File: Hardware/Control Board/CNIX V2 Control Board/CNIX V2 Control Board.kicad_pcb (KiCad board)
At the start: 2 copper layers, 165 x 51 mm, 108 parts, among them J1 EXT, J10 LED, J11 USB_C_Receptacle, J3 Tube Out, J4 EXT, J5 I2C_ext, J6 Prog, J7 HT, J8 GND, J9 GND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

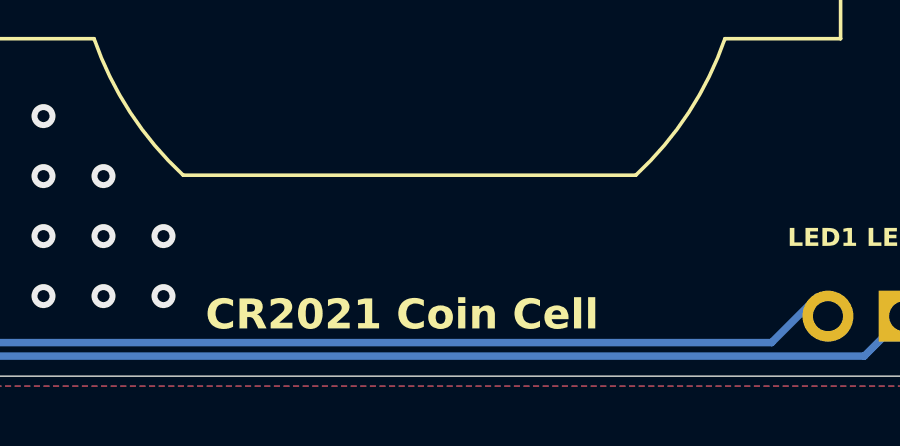
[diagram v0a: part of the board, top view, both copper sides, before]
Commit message: control board version 2.1.1 bump and added changelog
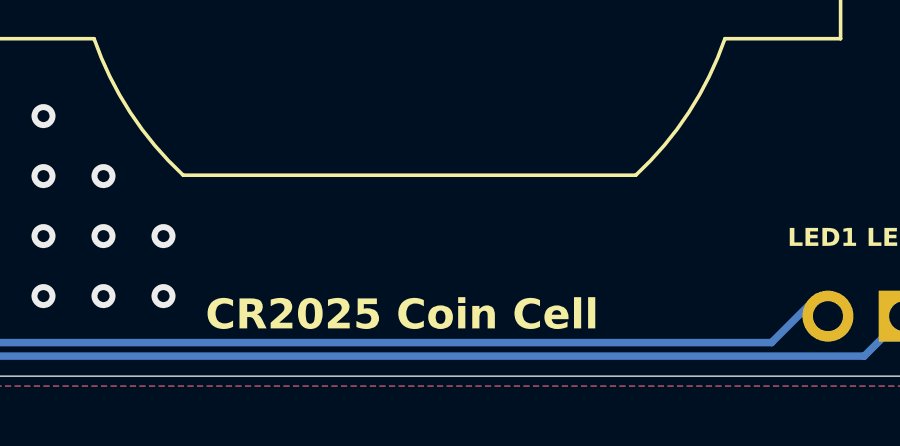
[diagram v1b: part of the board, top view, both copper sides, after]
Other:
- board text added: "CR2025 Coin Cell"
- board text removed: "CR2021 Coin Cell"
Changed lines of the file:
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@@
 	)
 	(paper "A4")
+	(title_block
+		(title "Nixie Tube Control Board")
+		(date "2026-01-13")
+		(rev "V2.1.1")
+		(company "C-Audio")
+	)
 	(layers
 		(0 "F.Cu" signal)
@@
 		)
 	)
-	(gr_text "CR2021 Coin Cell"
+	(gr_text "CR2025 Coin Cell"
 		(at 204.711051 129.531051 0)
 		(layer "F.SilkS" knockout)

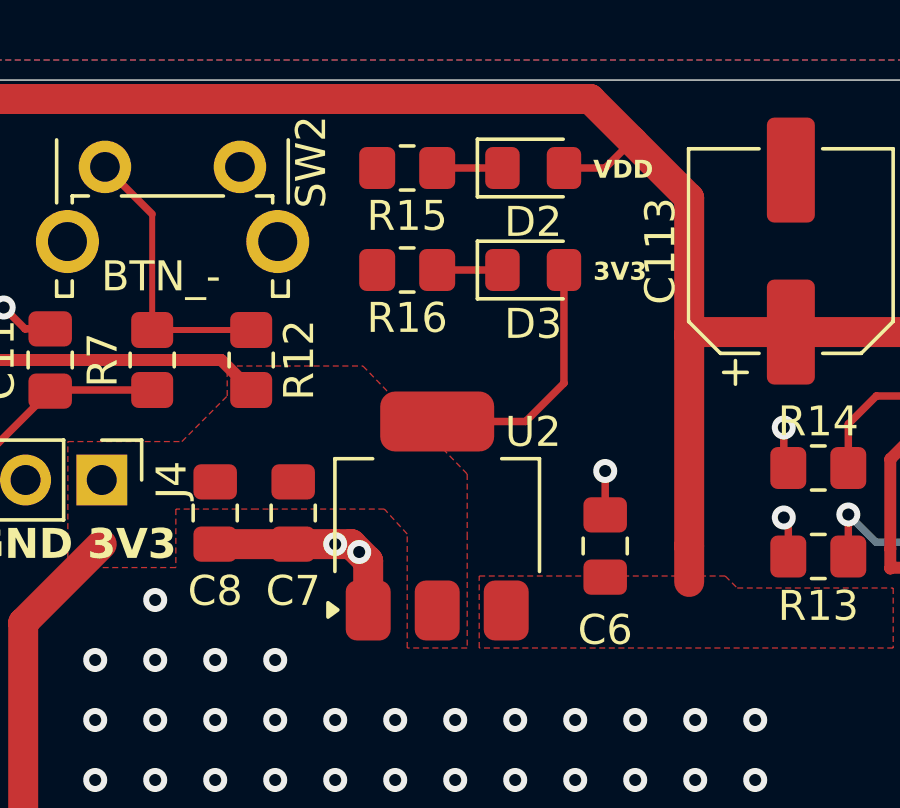
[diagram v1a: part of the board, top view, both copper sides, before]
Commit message: Version bump 2.2.0 -> new regulator and id system
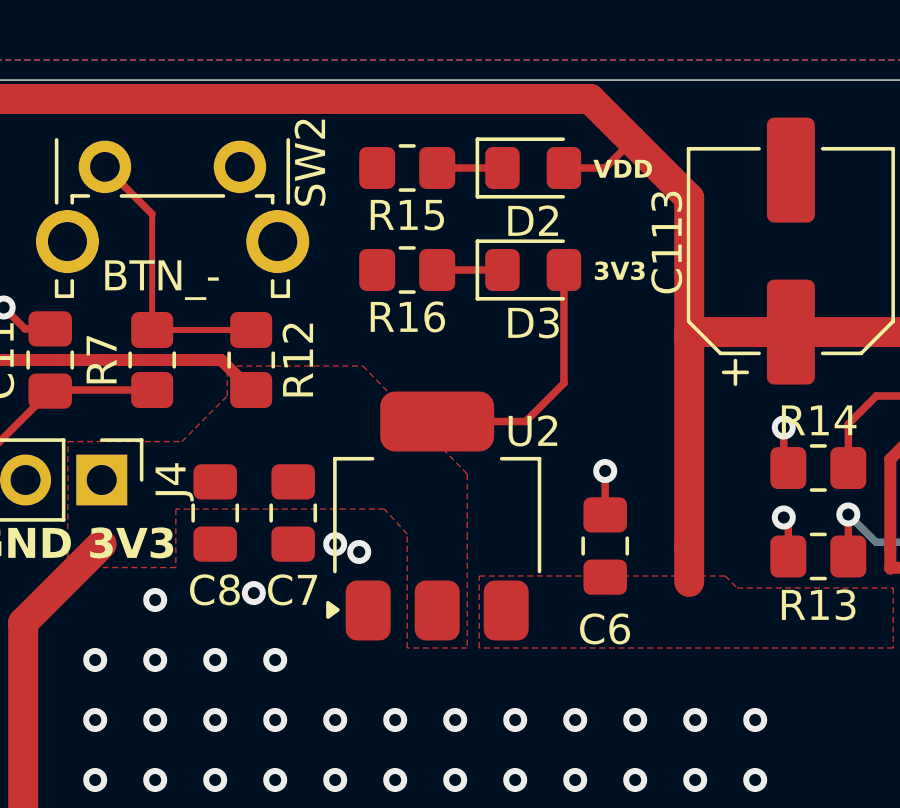
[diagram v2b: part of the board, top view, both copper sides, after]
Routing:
- net GND: track 63.8 -> 56.8 mm, vias 276 -> 277

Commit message: updated firmware: implemented DHT22 sensor, addon board id check, menu structure, led blink display
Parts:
- SW2: value SW_Plus -> SW_Minus
- SW4: value SW_Minus -> SW_Plus
- U2: value AMS1117-3.3 -> AP7361C-33ER-13
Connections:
- net /PD2 renamed /id_bit0
- net /PD3 renamed /id_bit1
- C11 pad 1: /btn_plus -> /btn_minus
- C9 pad 1: /btn_minus -> /btn_plus
- R7 pad 1: /btn_plus -> /btn_minus
- R9 pad 1: /btn_minus -> /btn_plus
- U1 pad 16: /btn_plus -> /btn_minus
- U1 pad 18: /btn_minus -> /btn_plus
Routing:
- net /btn_plus: track 36.9 -> 19.1 mm
- net /btn_minus: track 19.1 -> 36.9 mm
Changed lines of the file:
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@@
 	(net 79 "Net-(D102-A)")
 	(net 80 "Net-(D103-K)")
-	(net 81 "/PD2")
-	(net 82 "/PD3")
+	(net 81 "/id_bit0")
+	(net 82 "/id_bit1")
 	(footprint "TestPoint:TestPoint_Pad_D1.5mm"
 		(layer "F.Cu")
@@
 			(layers "F.Cu" "F.Mask" "F.Paste")
 			(roundrect_rratio 0.208333)
-			(net 13 "/btn_plus")
+			(net 15 "/btn_minus")
 			(pintype "passive")
 		)
@@
 			(layers "F.Cu" "F.Mask" "F.Paste")
 			(roundrect_rratio 0.212766)
-			(net 13 "/btn_plus")
+			(net 15 "/btn_minus")
 			(pintype "passive")
 		)
@@
 			)
 		)
-		(property "Value" "SW_Plus"
+		(property "Value" "SW_Minus"
 			(at 2.25 5.38988 0)
 			(layer "F.Fab")
@@
 			(layers "F.Cu" "F.Mask" "F.Paste")
 			(roundrect_rratio 0.212766)
-			(net 15 "/btn_minus")
+			(net 13 "/btn_plus")
 			(pintype "passive")
 		)
@@
 			(layers "F.Cu" "F.Mask" "F.Paste")
 			(roundrect_rratio 0.208333)
-			(net 15 "/btn_minus")
+			(net 13 "/btn_plus")
 			(pintype "passive")
 		)
@@
 			(layers "F.Cu" "F.Mask" "F.Paste")
 			(roundrect_rratio 0.25)
-			(net 13 "/btn_plus")
+			(net 15 "/btn_minus")
 			(pinfunction "PA5")
 			(pintype "bidirectional")
@@
 			(layers "F.Cu" "F.Mask" "F.Paste")
 			(roundrect_rratio 0.25)
-			(net 15 "/btn_minus")
+			(net 13 "/btn_plus")
 			(pinfunction "PA7")
 			(pintype "bidirectional")
@@
 			(layers "F.Cu" "F.Mask" "F.Paste")
 			(roundrect_rratio 0.25)
-			(net 81 "/PD2")
+			(net 81 "/id_bit0")
 			(pinfunction "PD2")
 			(pintype "bidirectional")
@@
 			(layers "F.Cu" "F.Mask" "F.Paste")
 			(roundrect_rratio 0.25)
-			(net 82 "/PD3")
+			(net 82 "/id_bit1")
 			(pinfunction "PD3")
 			(pintype "bidirectional")
@@
 			)
 		)
-		(property "Value" "SW_Minus"
+		(property "Value" "SW_Plus"
 			(at 2.25 5.38988 0)
 			(layer "F.Fab")
@@
 			)
 		)
-		(property "Value" "AMS1117-3.3"
+		(property "Value" "AP7361C-33ER-13"
 			(at 0 4.500001 90)
 			(layer "F.Fab")
@@
 			)
 		)
-		(property "Datasheet" "http://www.advanced-monolithic.com/pdf/ds1117.pdf"
+		(property "Datasheet" "https://www.mouser.de/datasheet/3/175/1/AP7361C.pdf"
 			(at 0 0 90)
 			(unlocked yes)
@@
 			)
 		)
-		(property "Description" "1A Low Dropout regulator, positive, 3.3V fixed output, SOT-223"
+		(property "Description" "The AP7361C is a 1A, adjustable and fixed output voltage, ultra-low dropout linear regulator with enable. The device includes pass element, error amplifier, band-gap reference, current limit and thermal shutdown circuitry. The device is turned on when EN pin is set to logic high level."
 			(at 0 0 90)
 			(unlocked yes)
@@
 			)
 		)
-		(property "Mouser-Nr." ""
+		(property "Mouser-Nr." "621-AP7361C-33ER-13 "
 			(at 0 0 90)
 			(unlocked yes)
@@
 			(layers "*.Cu" "*.Mask")
 			(remove_unused_layers no)
-			(net 81 "/PD2")
+			(net 81 "/id_bit0")
 			(pinfunction "Pin_3")
 			(pintype "passive")
@@
 			(layers "*.Cu" "*.Mask")
 			(remove_unused_layers no)
-			(net 82 "/PD3")
+			(net 82 "/id_bit1")
 			(pinfunction "Pin_4")
 			(pintype "passive")
@@
 	)
 	(segment
-		(start 176.622447 92.156051)
-		(end 176.311051 92.467447)
-		(width 0.25)
-		(layer "F.Cu")
-		(net 13)
-	)
-	(segment
-		(start 176.311051 103.498817)
-		(end 174.138266 105.671602)
+		(start 174.811051 91.831051)
+		(end 175.411051 92.431051)
 		(width 0.25)
 		(layer "F.Cu")
@@
 	)
 	(segment
-		(start 198.211051 90.331051)
-		(end 194.848551 90.331051)
+		(start 171.411051 90.368551)
+		(end 174.773551 90.368551)
 		(width 0.25)
 		(layer "F.Cu")
@@
 	)
 	(segment
-		(start 193.023551 92.156051)
-		(end 176.622447 92.156051)
+		(start 174.773551 90.368551)
+		(end 174.811051 90.331051)
 		(width 0.25)
 		(layer "F.Cu")
@@
 	)
 	(segment
-		(start 176.311051 92.467447)
-		(end 176.311051 103.498817)
+		(start 175.411051 102.984605)
+		(end 173.43116 104.964496)
 		(width 0.25)
 		(layer "F.Cu")
@@
 	)
 	(segment
-		(start 194.848551 90.331051)
-		(end 194.811051 90.368551)
+		(start 174.811051 90.331051)
+		(end 174.811051 91.831051)
 		(width 0.25)
 		(layer "F.Cu")
@@
 	)
 	(segment
-		(start 194.811051 90.368551)
-		(end 193.023551 92.156051)
+		(start 175.411051 92.431051)
+		(end 175.411051 102.984605)
 		(width 0.25)
 		(layer "F.Cu")
@@
 	)
 	(segment
-		(start 174.811051 91.831051)
-		(end 175.411051 92.431051)
+		(start 176.622447 92.156051)
+		(end 176.311051 92.467447)
 		(width 0.25)
 		(layer "F.Cu")
@@
 	)
 	(segment
-		(start 171.411051 90.368551)
-		(end 174.773551 90.368551)
+		(start 176.311051 103.498817)
+		(end 174.138266 105.671602)
 		(width 0.25)
 		(layer "F.Cu")
@@
 	)
 	(segment
-		(start 174.773551 90.368551)
-		(end 174.811051 90.331051)
+		(start 198.211051 90.331051)
+		(end 194.848551 90.331051)
 		(width 0.25)
 		(layer "F.Cu")
@@
 	)
 	(segment
-		(start 175.411051 102.984605)
-		(end 173.43116 104.964496)
+		(start 193.023551 92.156051)
+		(end 176.622447 92.156051)
 		(width 0.25)
 		(layer "F.Cu")
@@
 	)
 	(segment
-		(start 174.811051 90.331051)
-		(end 174.811051 91.831051)
+		(start 176.311051 92.467447)
+		(end 176.311051 103.498817)
 		(width 0.25)
 		(layer "F.Cu")
@@
 	)
 	(segment
-		(start 175.411051 92.431051)
-		(end 175.411051 102.984605)
+		(start 194.848551 90.331051)
+		(end 194.811051 90.368551)
+		(width 0.25)
+		(layer "F.Cu")
+		(net 15)
+	)
+	(segment
+		(start 194.811051 90.368551)
+		(end 193.023551 92.156051)
 		(width 0.25)
 		(layer "F.Cu")

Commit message: control board: added ht-psu enable jumper
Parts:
- added J100: HT_en, Connector_PinHeader_2.54mm:PinHeader_1x02_P2.54mm_Vertical, F.Cu at (101.5, 84.2)
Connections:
- D103 pad 2: /EN -> /~{EN}
- R100 pad 1: /EN -> Net-(J100-Pin_1)
- TP3 pad 1: /EN -> /~{EN}
- U1 pad 11: /EN -> /~{EN}
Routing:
- net /EN: track 108.1 -> 0.00 mm, vias 2 -> 0
- net /~{EN}: track 0.00 -> 107.3 mm, vias 0 -> 2
- net Net-(J100-Pin_1): track 0.00 -> 5.86 mm
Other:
- board text added: "EN_Enable"

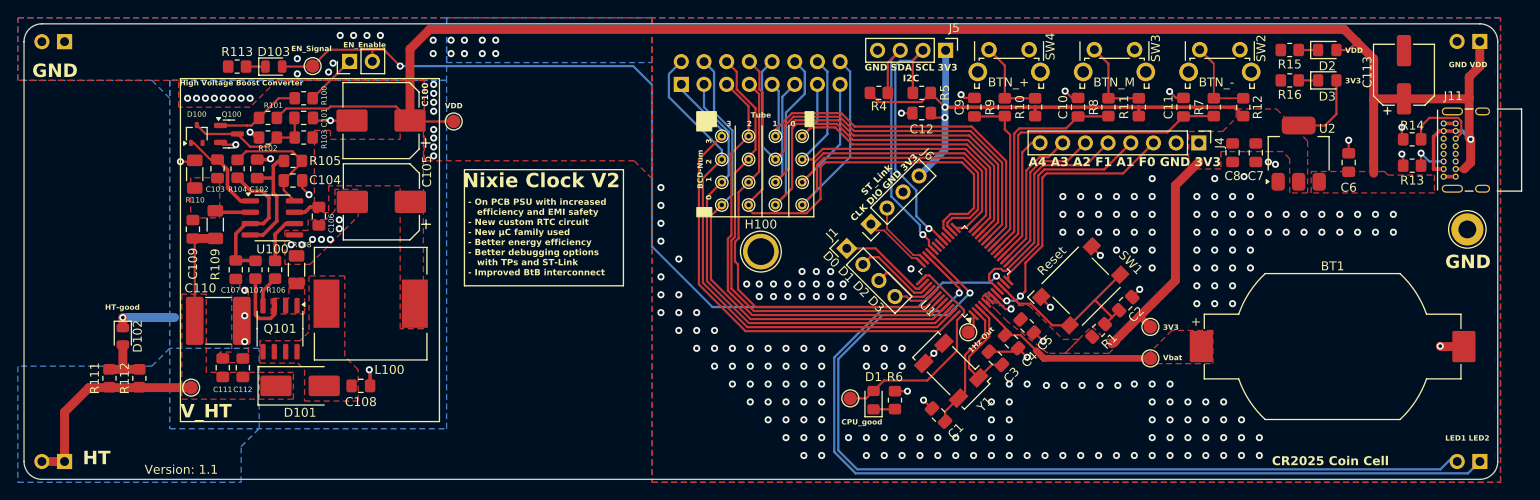
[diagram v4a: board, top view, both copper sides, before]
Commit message: finalized V2 and cleaned up Silkscreen
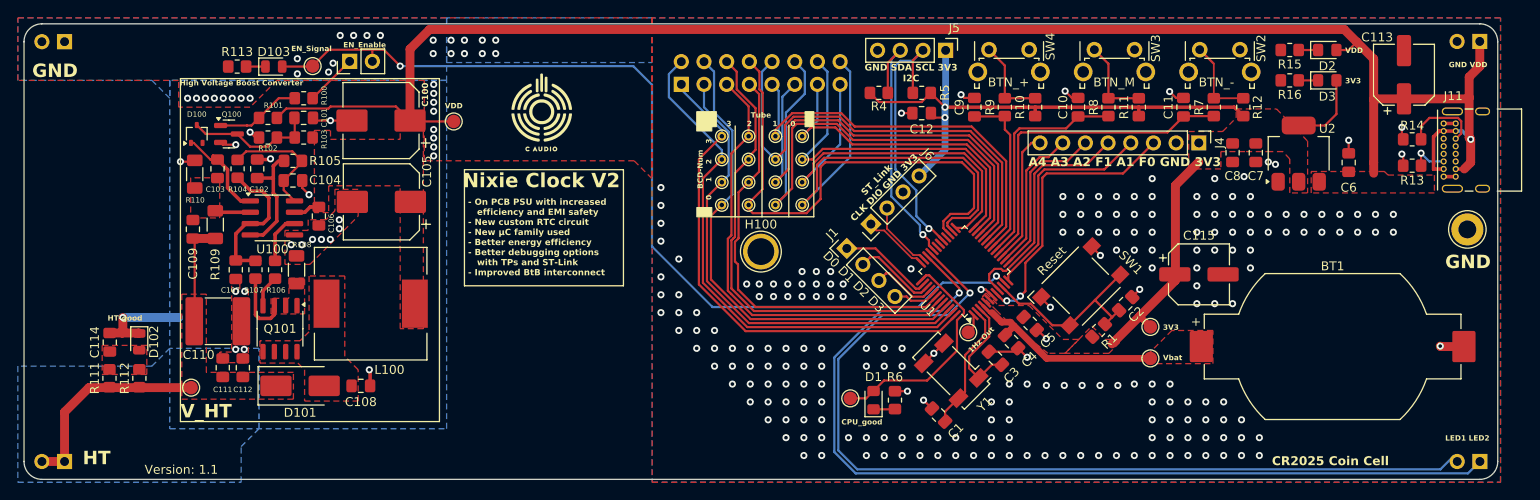
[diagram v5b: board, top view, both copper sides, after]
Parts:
- added C114: 100n 250V, Capacitor_SMD:C_0805_2012Metric_Pad1.18x1.45mm_HandSolder, F.Cu at (74.6, 115.7)
- added C115: 100u 16V, Capacitor_SMD:CP_Elec_6.3x7.7, F.Cu at (196.6, 108.0)
- added G***: LOGO, Logos:C Audio Logo 15mm, F.Cu at (123.0, 89.8)
- moved D102 1.94 mm to (77.9, 115.6)
- moved C5 0.44 mm to (177.7, 113.5)
- moved C110 0.07 mm to (86.7, 113.3)
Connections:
- net Net-(D102-A) renamed /HV Power Supply/LED_ht
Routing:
- net /HV Power Supply/LED_ht: track 6.11 -> 0.00 mm
- net GND: track 56.8 -> 60.1 mm, vias 277 -> 274
- net /Vbat: track 21.7 -> 22.6 mm
- added copper zone on F.Cu, net /HV Power Supply/LED_ht
